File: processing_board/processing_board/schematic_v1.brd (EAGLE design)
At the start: 72.4 x 58.1 mm, 20 parts, among them Q1 BSS138, Q2 BSS138

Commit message: modified shcematic and board
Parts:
- added J3: (no value), SparkFun-Connectors:1X04
- moved C5 84.7 mm to (14.0, 35.6)
- moved C6 84.7 mm to (17.8, 35.6)
- moved Q1 84.7 mm to (8.89, 38.1)
- moved Q2 84.7 mm to (2.54, 38.1)
- moved R1 84.7 mm to (2.54, 31.8)
- moved R2 84.7 mm to (2.54, 27.9)
- moved R3 84.7 mm to (2.54, 24.1)
- moved R4 84.7 mm to (2.54, 20.3)
- moved U$3 84.7 mm to (16.5, 41.9)
- moved C1 69.2 mm to (19.1, 30.5)
- moved C4 69.2 mm to (19.1, 26.7)
- moved JP1 69.1 mm to (44.5, 49.5)
- moved J1 56.7 mm to (10.2, 49.5)
- moved J2 56.4 mm to (2.54, 49.5)
- moved C2 48.3 mm to (15.2, 22.9)
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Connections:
- removed net N$11: Q2.2, R3.1
- removed net N$2: Q1.2, R2.1
- removed net VDD: C2.1, C3.2, U$1.VIN
- new net CAN_RX: J3.3, Q1.2, R2.1
- new net CAN_TX: J3.2, Q2.2, R3.1
- net +5V: now also C2.1, C3.2, J3.1, U$1.VIN
- net 3.3V: no longer U$1.3.3V
- net GND: now also J3.4
- net TEENSY_3.3V: now also U$1.3.3V
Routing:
- net GND: track 69.9 -> 0.50 mm

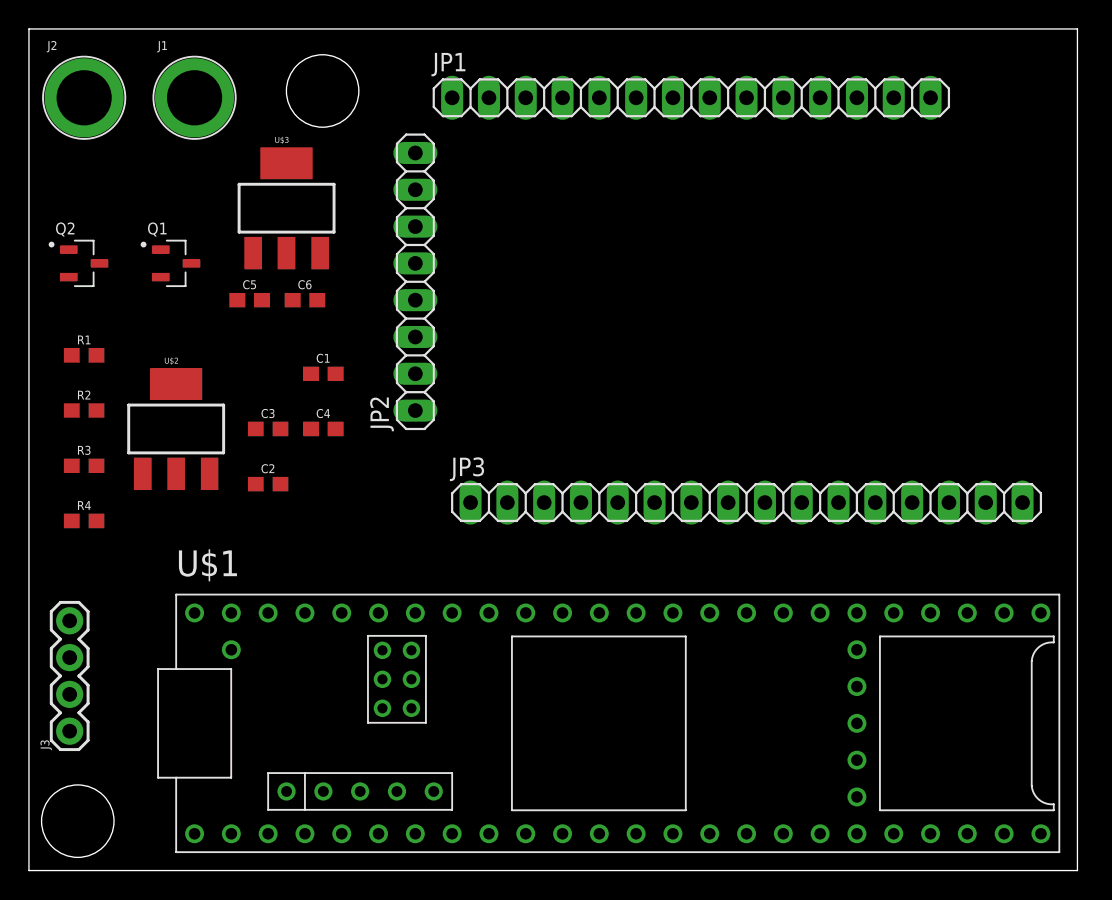
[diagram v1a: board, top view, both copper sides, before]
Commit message: routed to radio mod
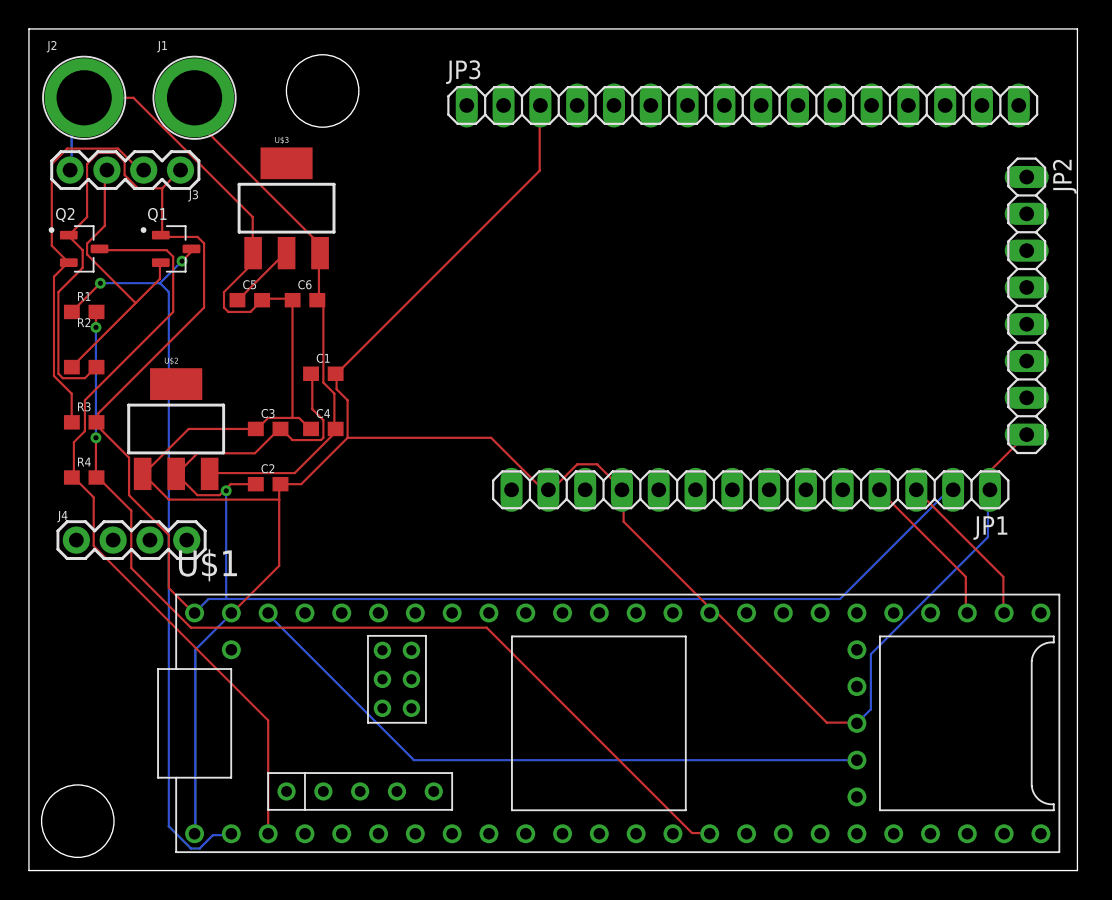
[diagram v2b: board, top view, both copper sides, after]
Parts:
- added J4: (no value), SparkFun-Connectors:1X04
- moved JP2 42.2 mm to (67.6, 35.2), turned to 270 degrees
- moved J3 39.5 mm to (9.19, 44.5), turned to 180 degrees
- moved JP3 27.4 mm to (48.0, 49.0)
- moved JP1 27.4 mm to (48.5, 22.5), turned to 180 degrees
- moved R1 3.00 mm to (2.54, 34.8)
- moved R2 3.00 mm to (2.54, 30.9)
- moved R3 3.00 mm to (2.54, 27.1)
- moved R4 3.00 mm to (2.54, 23.3)
- moved Q1 1.00 mm to (8.89, 39.1)
- moved Q2 1.00 mm to (2.54, 39.1)
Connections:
- new net 1: J4.1
- new net 2: J4.2
- new net N$1: JP1.4, U$1.D35
- new net N$2: JP1.3, U$1.D34
- net +5V: now also JP1.2
- net GND: now also JP1.1, JP1.11, JP1.13, JP2.8, JP3.3
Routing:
- net GND: track 0.50 -> 198.3 mm
- net +5V: track 0.00 -> 152.6 mm, vias 0 -> 1
- net TEENSY_3.3V: track 0.00 -> 66.3 mm, vias 0 -> 2
- net N$12: track 0.00 -> 53.7 mm
- net N$3: track 0.00 -> 53.4 mm, vias 0 -> 2
- net 3.3V: track 0.22 -> 45.1 mm
- net +15V: track 0.00 -> 37.2 mm
- net CAN_TX: track 0.00 -> 26.7 mm
- net CAN_RX: track 0.00 -> 20.9 mm
- net N$1: track 0.00 -> 11.0 mm
- net N$2: track 0.00 -> 11.0 mm
- net +3.3V: track 0.00 -> 4.77 mm

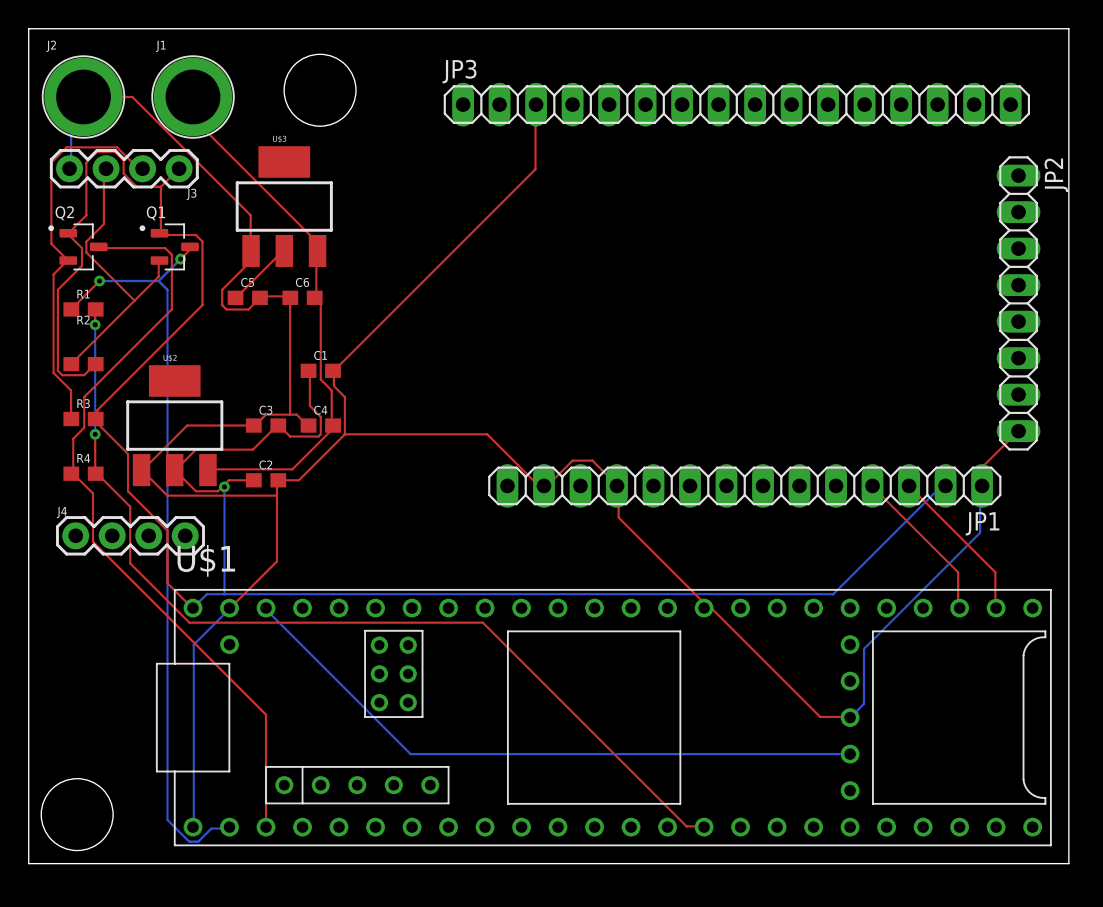
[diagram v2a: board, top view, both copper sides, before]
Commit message: added LED
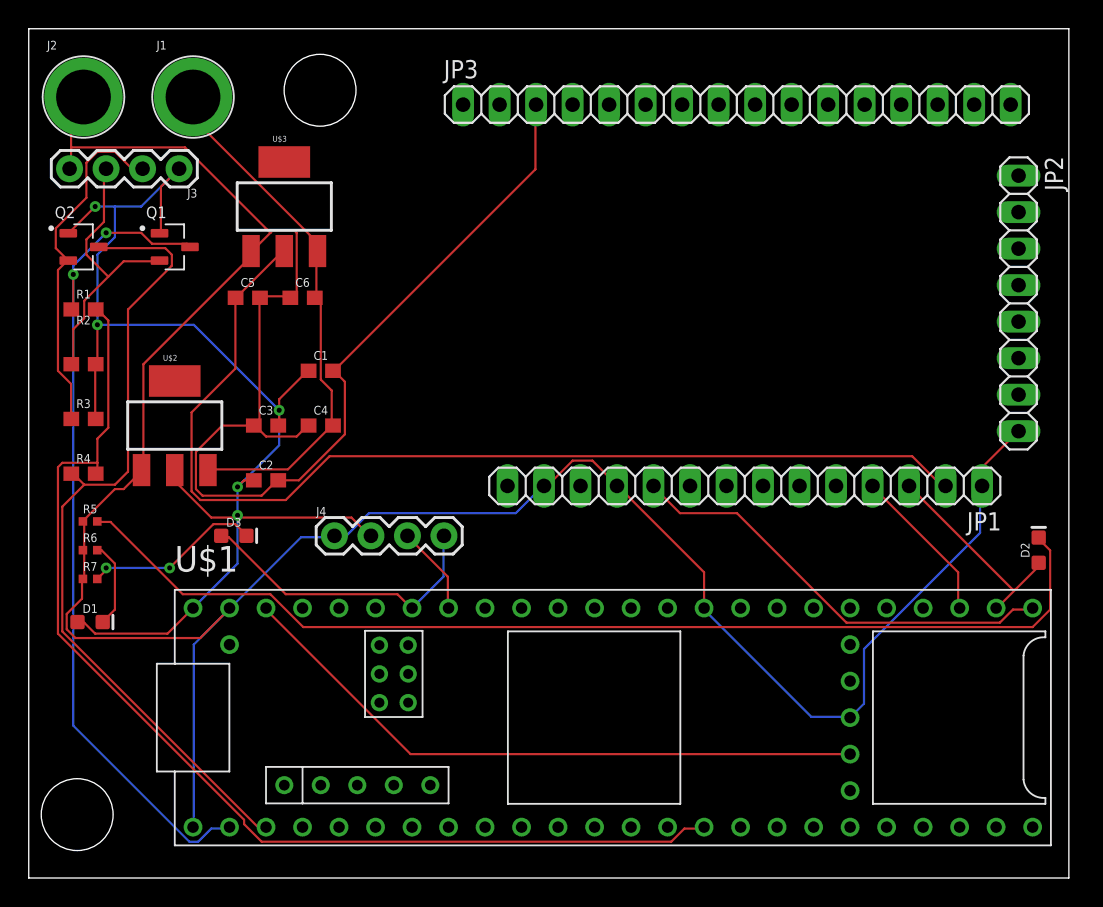
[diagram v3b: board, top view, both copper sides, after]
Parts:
- added D1: RED, SparkFun-LED:LED-0603
- added D2: GREEN, SparkFun-LED:LED-0603
- added D3: BLUE, SparkFun-LED:LED-0603
- added R5, R6, R7: 220KOHM-0402T-1/16W-1%, SparkFun-Resistors:0402-TIGHT
- moved J4 18.0 mm to (20.0, 19.0)
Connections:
- removed net 1: J4.1
- removed net 2: J4.2
- new net N$4: D2.C, R5.2
- new net N$5: J4.3, U$1.D19/A5
- new net N$6: D3.A, J4.4, U$1.D20/A6
- new net N$7: D1.C, R6.2
- new net N$8: D3.C, R7.2
- new net N$9: JP1.10, U$1.D33
- net +3.3V: now also JP1.2
- net +5V: now also D1.A, J4.2; no longer JP1.2
- net GND: now also J4.1, R5.1, R6.1, R7.1
- net N$2: now also D2.A
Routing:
- net N$4: track 0.00 -> 75.2 mm
- net +3.3V: track 4.77 -> 74.3 mm
- net +5V: track 152.6 -> 92.7 mm, vias 1 -> 5
- net GND: track 198.3 -> 237.0 mm
- net N$9: track 0.00 -> 30.8 mm
- net N$6: track 0.00 -> 21.3 mm
- net N$8: track 0.00 -> 12.4 mm, vias 0 -> 2
- net TEENSY_3.3V: track 66.3 -> 78.3 mm, vias 2 -> 0
- net N$5: track 0.00 -> 6.21 mm
- net N$7: track 0.00 -> 6.03 mm
- net N$3: track 53.4 -> 58.6 mm
- net N$2: track 11.0 -> 14.8 mm
- net N$12: track 53.7 -> 57.0 mm
- net CAN_TX: track 26.7 -> 24.5 mm
- net CAN_RX: track 20.9 -> 19.9 mm
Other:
- board size 72.4 x 58.1 mm -> 72.4 x 59.1 mm
